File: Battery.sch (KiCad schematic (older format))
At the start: 12 parts, among them IC1 TPS61201

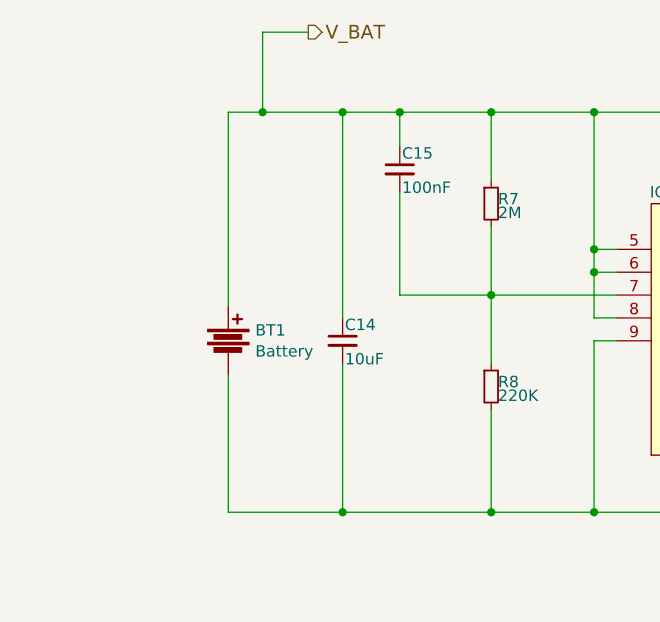
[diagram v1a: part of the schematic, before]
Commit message: moved battery input and fixed dodgy ground plane
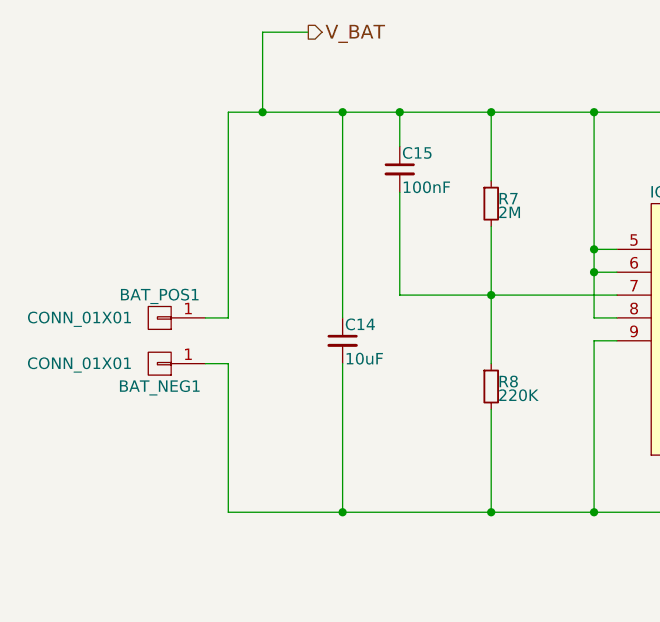
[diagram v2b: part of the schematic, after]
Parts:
- removed BT1: Battery, Pin_Headers:Pin_Header_Straight_1x02, symbol Battery
- added BAT_NEG1, BAT_POS1: CONN_01X01, Measurement_Points:Measurement_Point_Round-TH_Small, symbol CONN_01X01
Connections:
- net GND: now also BAT_NEG1.1 (P1)
- net V_BAT: now also BAT_POS1.1 (P1)
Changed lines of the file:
@@
 $EndDescr
-$Comp
-L Battery BT1
-U 1 1 56DB96F7
-P 2400 3800
-F 0 "BT1" H 2518 3846 50  0000 L CNN
-F 1 "Battery" H 2518 3754 50  0000 L CNN
-F 2 "Pin_Headers:Pin_Header_Straight_1x02" V 2400 3840 50  0001 C CNN
-F 3 "" V 2400 3840 50  0000 C CNN
-	1    2400 3800
-	1    0    0    -1
-$EndComp
 $Comp
 L TPS61200 IC1
@@
 $EndComp
 $Comp
-L GND #PWR031
+L GND #PWR31
 U 1 1 56EB0875
 P 4700 4750
-F 0 "#PWR031" H 4700 4500 50  0001 C CNN
+F 0 "#PWR31" H 4700 4500 50  0001 C CNN
 F 1 "GND" H 4700 4600 50  0000 C CNN
 F 2 "" H 4700 4750 50  0000 C CNN
@@
 $EndComp
 $Comp
-L +3V3 #PWR032
+L +3V3 #PWR32
 U 1 1 56EB2DD1
 P 6650 3250
-F 0 "#PWR032" H 6650 3100 50  0001 C CNN
+F 0 "#PWR32" H 6650 3100 50  0001 C CNN
 F 1 "+3V3" H 6650 3390 50  0000 C CNN
 F 2 "" H 6650 3250 50  0000 C CNN
@@
 	5550 3400 5300 3400
 Wire Wire Line
-	2400 2800 2400 3650
+	2400 2800 2400 3700
 Wire Wire Line
 	3150 2800 3150 2950
@@
 	3150 3150 3150 3600
 Wire Wire Line
-	3550 4100 3550 4550
-Wire Wire Line
-	2400 3950 2400 4550
+	3550 4550 3550 4100
+Wire Wire Line
+	2400 3900 2400 4550
 Connection ~ 3550 4550
 Wire Wire Line
@@
 	2900 3900 2900 4550
 Connection ~ 2900 4550
+$Comp
+L CONN_01X01 BAT_POS1
+U 1 1 56F8DA89
+P 2100 3700
+F 0 "BAT_POS1" H 2100 3600 50  0000 C CNN
+F 1 "CONN_01X01" H 2450 3700 50  0000 C CNN
+F 2 "Measurement_Points:Measurement_Point_Round-TH_Small" H 2100 3700 50  0001 C CNN
+F 3 "" H 2100 3700 50  0000 C CNN
+	1    2100 3700
+	-1   0    0    1
+$EndComp
+$Comp
+L CONN_01X01 BAT_NEG1
+U 1 1 56F8DAE4
+P 2100 3900
+F 0 "BAT_NEG1" H 2100 4000 50  0000 C CNN
+F 1 "CONN_01X01" H 2450 3900 50  0000 C CNN
+F 2 "Measurement_Points:Measurement_Point_Round-TH_Small" H 2100 3900 50  0001 C CNN
+F 3 "" H 2100 3900 50  0000 C CNN
+	1    2100 3900
+	-1   0    0    1
+$EndComp
+Wire Wire Line
+	2400 3700 2300 3700
+Wire Wire Line
+	2300 3900 2400 3900
 $EndSCHEMATC

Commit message: Changed L3 to 0603, L2 to 3x3, Fixed P8 silk and made gerbers
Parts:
- L2: footprint Capacitors_SMD:C_0805 -> Inductors_NEOSID:Neosid_Inductor_SMS-ME3015
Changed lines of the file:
@@
 $EndComp
 $Comp
-L GND #PWR31
+L GND #PWR032
 U 1 1 56EB0875
 P 4700 4750
-F 0 "#PWR31" H 4700 4500 50  0001 C CNN
+F 0 "#PWR032" H 4700 4500 50  0001 C CNN
 F 1 "GND" H 4700 4600 50  0000 C CNN
 F 2 "" H 4700 4750 50  0000 C CNN
@@
 F 0 "L2" H 4700 2900 50  0000 C CNN
 F 1 "2.2uH" H 4700 2750 50  0000 C CNN
-F 2 "Capacitors_SMD:C_0805" H 4700 2800 50  0001 C CNN
+F 2 "Inductors_NEOSID:Neosid_Inductor_SMS-ME3015" H 4700 2800 50  0001 C CNN
 F 3 "" H 4700 2800 50  0000 C CNN
 	1    4700 2800
@@
 $EndComp
 $Comp
-L +3V3 #PWR32
+L +3V3 #PWR033
 U 1 1 56EB2DD1
 P 6650 3250
-F 0 "#PWR32" H 6650 3100 50  0001 C CNN
+F 0 "#PWR033" H 6650 3100 50  0001 C CNN
 F 1 "+3V3" H 6650 3390 50  0000 C CNN
 F 2 "" H 6650 3250 50  0000 C CNN

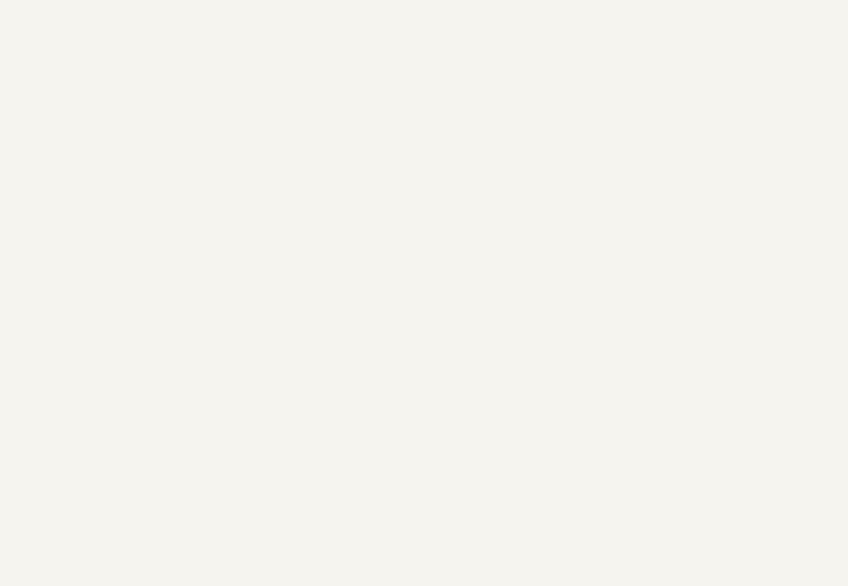
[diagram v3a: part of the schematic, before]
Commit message: Started work to add the power mux and USB connector
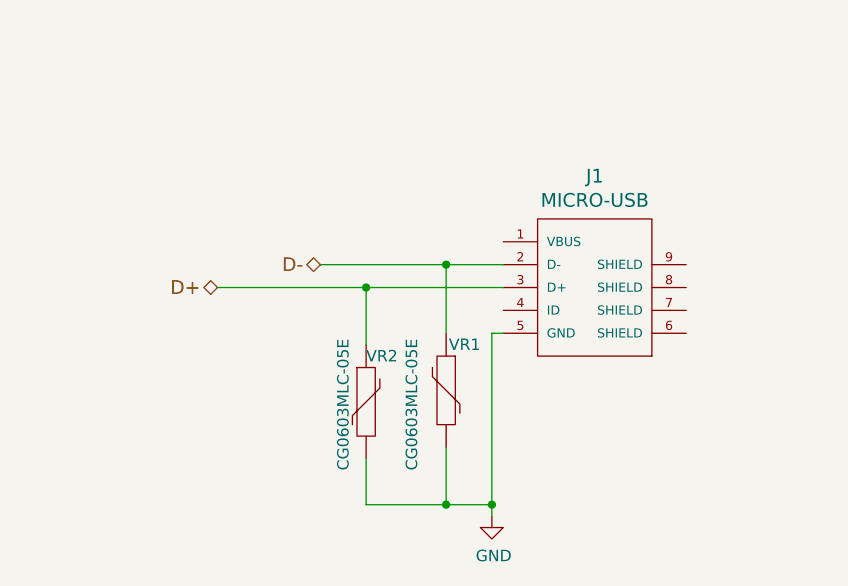
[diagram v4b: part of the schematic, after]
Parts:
- added J1: MICRO-USB, RocketScreamKicadLibrary:MICRO-USB, symbol MICRO-USB
- added VR1, VR2: CG0603MLC-05E, Capacitors_SMD:C_0603, symbol VR
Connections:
- net GND: now also J1.5 (GND), VR1.2, VR2.2
- new net D+: J1.3 (D+), VR2.1
- new net D-: J1.2 (D-), VR1.1
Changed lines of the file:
@@
 $EndComp
 $Comp
-L GND #PWR032
+L GND #PWR033
 U 1 1 56EB0875
 P 4700 4750
-F 0 "#PWR032" H 4700 4500 50  0001 C CNN
+F 0 "#PWR033" H 4700 4500 50  0001 C CNN
 F 1 "GND" H 4700 4600 50  0000 C CNN
 F 2 "" H 4700 4750 50  0000 C CNN
@@
 $EndComp
 $Comp
-L +3V3 #PWR033
+L +3V3 #PWR034
 U 1 1 56EB2DD1
 P 6650 3250
-F 0 "#PWR033" H 6650 3100 50  0001 C CNN
+F 0 "#PWR034" H 6650 3100 50  0001 C CNN
 F 1 "+3V3" H 6650 3390 50  0000 C CNN
 F 2 "" H 6650 3250 50  0000 C CNN
@@
 Wire Wire Line
 	2300 3900 2400 3900
+$Comp
+L MICRO-USB J1
+U 1 1 57013C4C
+P 5050 6250
+F 0 "J1" H 5050 6737 60  0000 C CNN
+F 1 "MICRO-USB" H 5050 6631 60  0000 C CNN
+F 2 "RocketScreamKicadLibrary:MICRO-USB" H 5050 5800 60  0001 C CNN
+F 3 "" H 5100 6450 60  0000 C CNN
+	1    5050 6250
+	-1   0    0    -1
+$EndComp
+$Comp
+L VR VR1
+U 1 1 570144F7
+P 4400 6700
+F 0 "VR1" H 4250 6900 50  0000 L CNN
+F 1 "CG0603MLC-05E" V 4550 6350 50  0000 L CNN
+F 2 "Capacitors_SMD:C_0603" V 4750 6250 50  0001 L CNN
+F 3 "" H 4400 6700 50  0000 C CNN
+	1    4400 6700
+	-1   0    0    -1
+$EndComp
+$Comp
+L VR VR2
+U 1 1 57014F94
+P 4050 6750
+F 0 "VR2" H 4050 6950 50  0000 L CNN
+F 1 "CG0603MLC-05E" V 3950 6450 50  0000 L CNN
+F 2 "Capacitors_SMD:C_0603" H 4138 6658 50  0001 L CNN
+F 3 "" H 4050 6750 50  0000 C CNN
+	1    4050 6750
+	1    0    0    -1
+$EndComp
+Text HLabel 3400 6250 0    60   BiDi ~ 0
+D+
+Text HLabel 3850 6150 0    60   BiDi ~ 0
+D-
+Wire Wire Line
+	4400 6150 4400 6450
+Wire Wire Line
+	3400 6250 4650 6250
+Wire Wire Line
+	4050 6250 4050 6500
+$Comp
+L GND #PWR?
+U 1 1 57015938
+P 4600 7250
+F 0 "#PWR?" H 4600 7000 50  0001 C CNN
+F 1 "GND" H 4608 7076 50  0000 C CNN
+F 2 "" H 4600 7250 50  0000 C CNN
+F 3 "" H 4600 7250 50  0000 C CNN
+	1    4600 7250
+	1    0    0    -1
+$EndComp
+Wire Wire Line
+	4400 6950 4400 7200
+Wire Wire Line
+	4600 6450 4600 7250
+Wire Wire Line
+	4050 7000 4050 7200
+Connection ~ 4600 7200
+Wire Wire Line
+	3850 6150 4650 6150
+Connection ~ 4400 6150
+Connection ~ 4050 6250
+Wire Wire Line
+	4050 7200 4600 7200
+Connection ~ 4400 7200
+Wire Wire Line
+	4650 6450 4600 6450
 $EndSCHEMATC

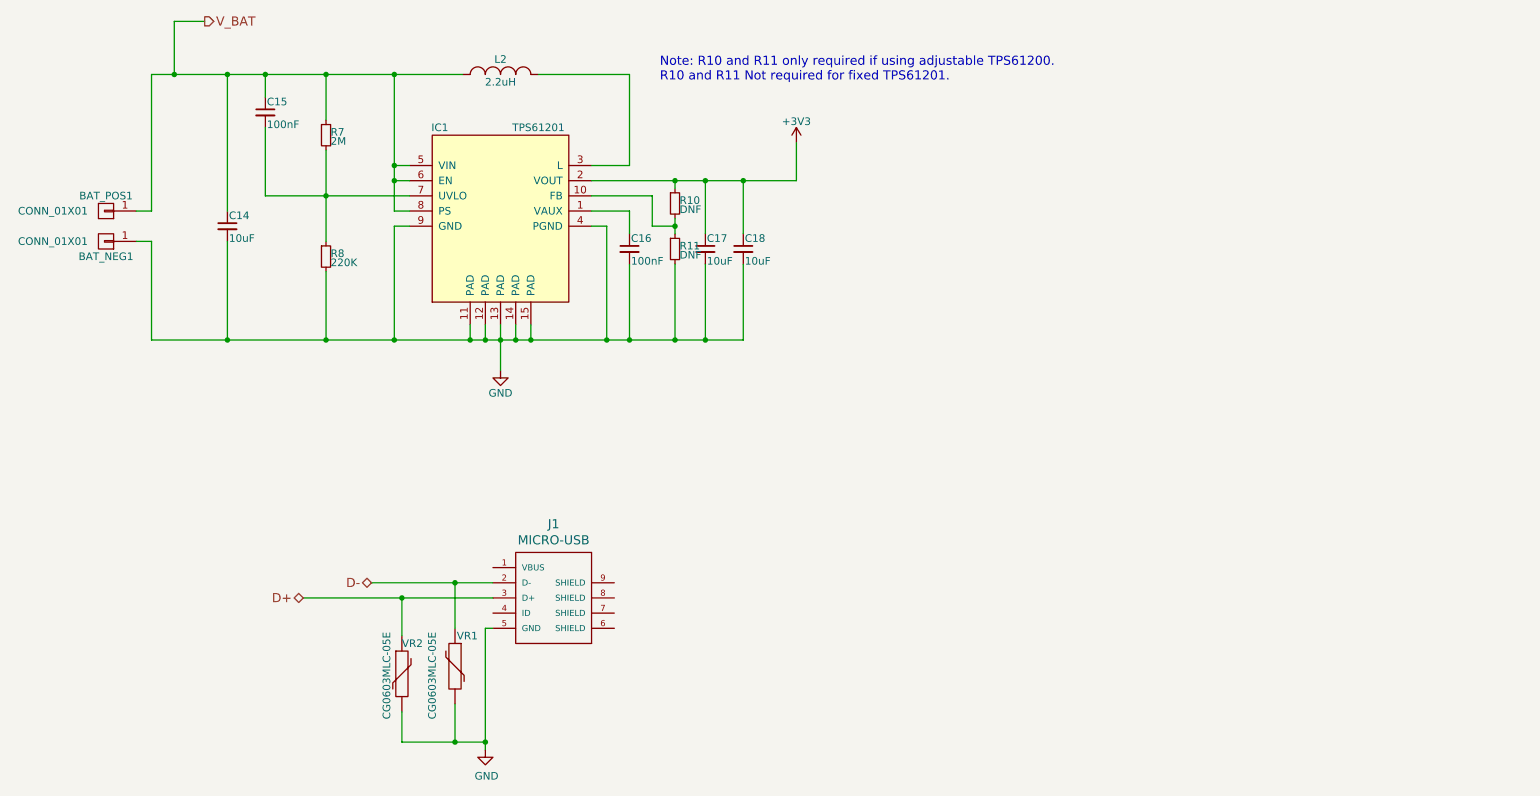
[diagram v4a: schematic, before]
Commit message: Added USB connector, diode or etc to layout@
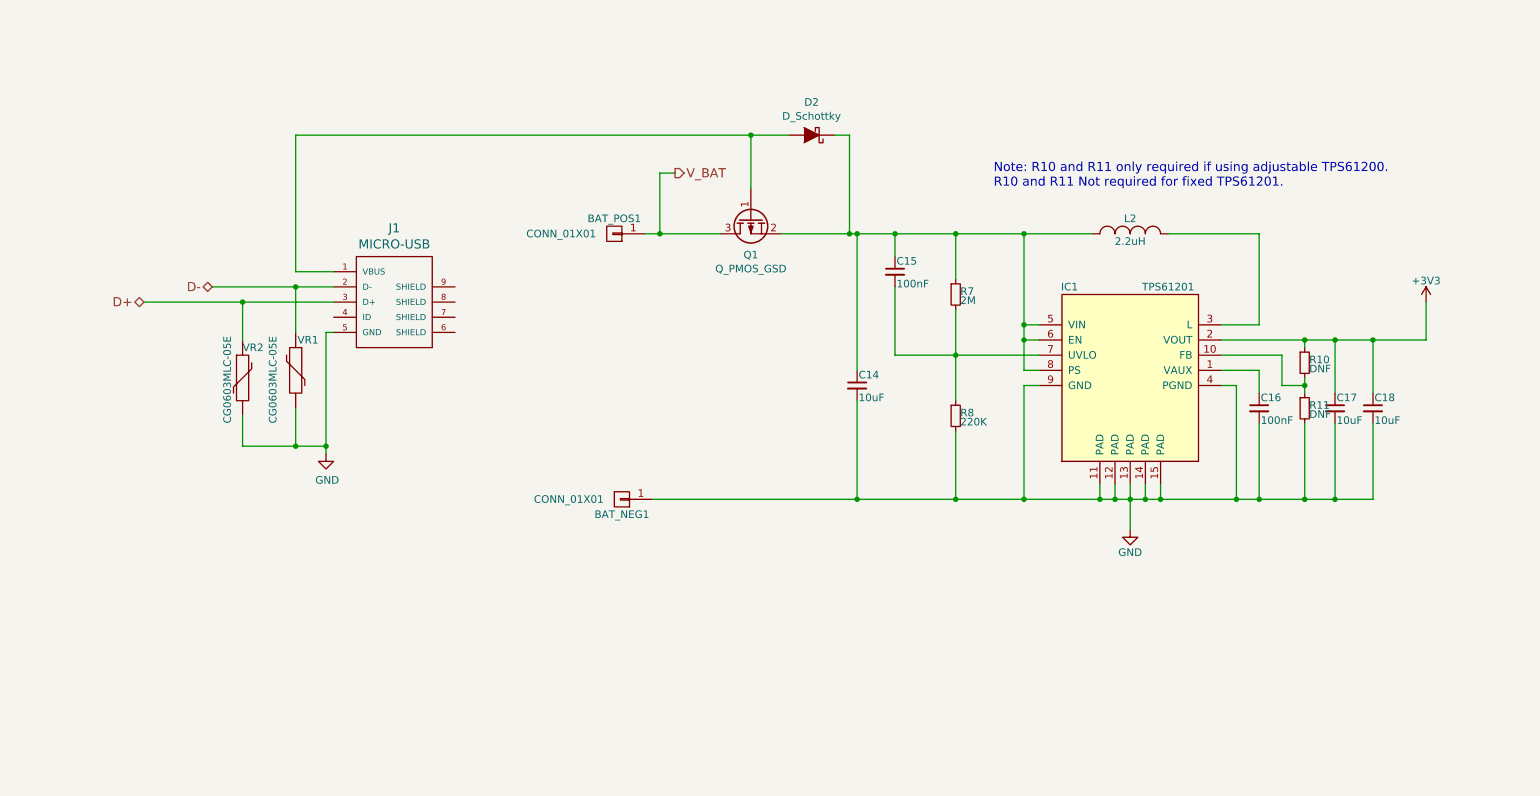
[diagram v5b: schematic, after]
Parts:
- added D2: D_Schottky, Diodes_SMD:SOD-323, symbol D_Schottky
- added Q1: Q_PMOS_GSD, TO_SOT_Packages_SMD:SOT-23, symbol Q_PMOS_GSD
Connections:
- net V_BAT: now also Q1.3 (D); no longer C14.1, C15.1, IC1.5 (VIN), IC1.6 (EN), IC1.8 (PS), L2.1, R7.1
- net at J1.1 (VBUS): now also D2.2 (A), Q1.1 (G)
- new net: C14.1, C15.1, D2.1 (K), IC1.5 (VIN), IC1.6 (EN), IC1.8 (PS), L2.1, Q1.2 (S), R7.1
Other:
- moved on the sheet: BAT_NEG1, BAT_POS1, C14, C15, C16, C17, C18, IC1, J1, L2, R10, R11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

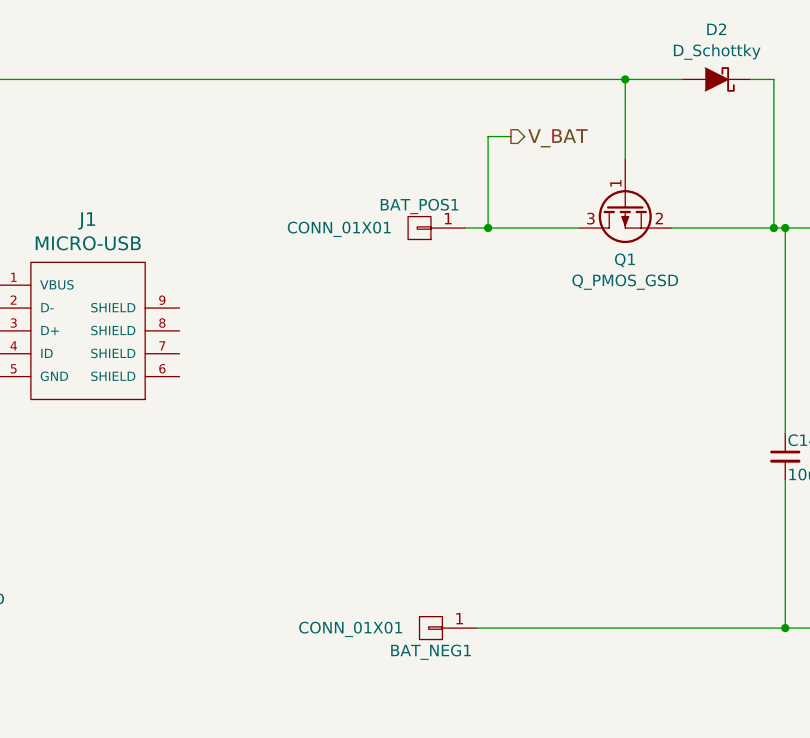
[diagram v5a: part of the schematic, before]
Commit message: Added USB monitoring resistors, still need to set values. Also added stitching vias and tried to clean up some layout
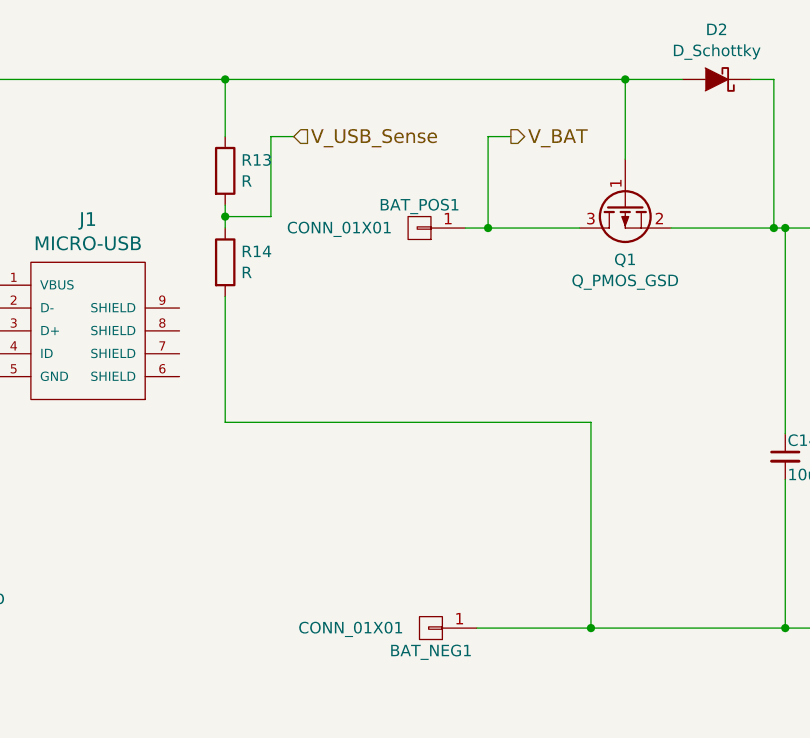
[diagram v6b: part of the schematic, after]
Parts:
- added R13, R14: R, Capacitors_SMD:C_0603, symbol R
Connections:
- net GND: now also R14.2
- net at D2.2 (A), J1.1 (VBUS), Q1.1 (G): now also R13.1
- new net V_USB_Sense: R13.2, R14.1
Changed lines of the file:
@@
 $EndComp
 $Comp
-L GND #PWR031
+L GND #PWR32
 U 1 1 56EB0875
 P 8850 5800
-F 0 "#PWR031" H 8850 5550 50  0001 C CNN
+F 0 "#PWR32" H 8850 5550 50  0001 C CNN
 F 1 "GND" H 8850 5650 50  0000 C CNN
 F 2 "" H 8850 5800 50  0000 C CNN
@@
 $EndComp
 $Comp
-L +3V3 #PWR032
+L +3V3 #PWR33
 U 1 1 56EB2DD1
 P 10800 4300
-F 0 "#PWR032" H 10800 4150 50  0001 C CNN
+F 0 "#PWR33" H 10800 4150 50  0001 C CNN
 F 1 "+3V3" H 10800 4440 50  0000 C CNN
 F 2 "" H 10800 4300 50  0000 C CNN
@@
 	3000 4300 3000 4550
 $Comp
-L GND #PWR033
+L GND #PWR31
 U 1 1 57015938
 P 3550 5300
-F 0 "#PWR033" H 3550 5050 50  0001 C CNN
+F 0 "#PWR31" H 3550 5050 50  0001 C CNN
 F 1 "GND" H 3558 5126 50  0000 C CNN
 F 2 "" H 3550 5300 50  0000 C CNN
@@
 	7000 3200 7000 3850
 Connection ~ 7000 3850
+$Comp
+L R R13
+U 1 1 5733A37D
+P 4600 3600
+F 0 "R13" H 4670 3646 50  0000 L CNN
+F 1 "R" H 4670 3554 50  0000 L CNN
+F 2 "Capacitors_SMD:C_0603" V 4530 3600 50  0001 C CNN
+F 3 "" H 4600 3600 50  0000 C CNN
+	1    4600 3600
+	1    0    0    -1
+$EndComp
+$Comp
+L R R14
+U 1 1 5733A3C7
+P 4600 4000
+F 0 "R14" H 4670 4046 50  0000 L CNN
+F 1 "R" H 4670 3954 50  0000 L CNN
+F 2 "Capacitors_SMD:C_0603" V 4530 4000 50  0001 C CNN
+F 3 "" H 4600 4000 50  0000 C CNN
+	1    4600 4000
+	1    0    0    -1
+$EndComp
+Wire Wire Line
+	4600 3200 4600 3450
+Connection ~ 4600 3200
+Wire Wire Line
+	4600 3750 4600 3850
+Wire Wire Line
+	4600 4150 4600 4700
+Wire Wire Line
+	4600 4700 6200 4700
+Wire Wire Line
+	6200 4700 6200 5600
+Connection ~ 6200 5600
+Text HLabel 4900 3450 2    60   Input ~ 0
+V_USB_Sense
+Wire Wire Line
+	4600 3800 4800 3800
+Wire Wire Line
+	4800 3800 4800 3450
+Wire Wire Line
+	4800 3450 4900 3450
+Connection ~ 4600 3800
 $EndSCHEMATC
